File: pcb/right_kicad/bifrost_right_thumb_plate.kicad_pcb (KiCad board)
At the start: 2 copper layers, 47.3 x 36.4 mm, 2 parts

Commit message: Update PCB and case designs
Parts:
- PH44: value R0C43 -> 1U
- PH45: value R0C44 -> 1U
- moved PH45 202.1 mm to (99.2, 59.5), turned to 0 degrees
- moved PH44 200.9 mm to (79.8, 60.6), turned to 6.179 degrees
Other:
- board size 47.3 x 36.4 mm -> 49.9 x 21.9 mm
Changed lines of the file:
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@@
 		(legacy_teardrops no)
 	)
-	(paper "A3")
+	(paper "A5")
 	(layers
 		(0 "F.Cu" signal)
@@
 		(capping no)
 		(filling no)
-		(zone_defaults)
-		(grid_origin -102.4605 73.281)
 		(pcbplotparams
 			(layerselection 0x00000000_00000000_55555555_5755f5ff)
@@
 	(footprint "Smidr:Plate_Smidr_Key_Hole"
 		(layer "F.Cu")
-		(at -120.0205 81.69 28.679)
+		(at 79.77744 60.580232 6.179)
 		(descr "Smidr keyboard plate key hole, center-origin template")
 		(tags "Smidr keyboard plate key hole center origin")
 		(property "Reference" "PH44"
-			(at 0 -11.025 0)
+			(at 0.000001 -11.025 6.179)
 			(layer "F.SilkS")
 			(hide yes)
@@
 			)
 		)
-		(property "Value" "R0C43"
-			(at 0 11.025 0)
+		(property "Value" "1U"
+			(at 0 8.1 6.179)
+			(layer "F.Fab")
+			(effects
+				(font
+					(size 1 1)
+					(thickness 0.15)
+				)
+			)
+		)
+		(property "Datasheet" ""
+			(at 0 0 6.179)
 			(layer "F.Fab")
 			(hide yes)
 			(effects
 				(font
-					(size 1 1)
-					(thickness 0.15)
-				)
-			)
-		)
-		(property "Datasheet" ""
-			(at 0 0 0)
-			(layer "F.Fab")
-			(hide yes)
-			(effects
-				(font
 					(size 1.27 1.27)
 					(thickness 0.15)
@@
 		)
 		(property "Description" ""
-			(at 0 0 0)
+			(at 0 0 6.179)
 			(layer "F.Fab")
 			(hide yes)
@@
 		)
 		(fp_line
-			(start -7.05 6.550002)
+			(start -7.05 6.550003)
 			(end -7.05 -6.55)
 			(stroke
@@
 			(start -6.55 7.05)
 			(mid -6.903552 6.903554)
-			(end -7.05 6.550002)
+			(end -7.05 6.550003)
 			(stroke
 				(width 0.05)
@@
 			(start 6.55 -7.05)
 			(mid 6.903552 -6.903554)
-			(end 7.05 -6.550002)
+			(end 7.05 -6.550003)
 			(stroke
 				(width 0.05)
@@
 			(start 7.05 6.55)
 			(mid 6.903554 6.903552)
-			(end 6.550002 7.05)
+			(end 6.550003 7.05)
 			(stroke
 				(width 0.05)
@@
 			)
 			(stroke
-				(width 0.05)
-				(type solid)
-			)
-			(fill no)
-			(layer "F.CrtYd")
-		)
-		(fp_poly
-			(pts
-				(xy -9.525 -9.525) (xy 9.525 -9.525) (xy 9.525 9.525) (xy -9.525 9.525)
-			)
-			(stroke
 				(width 0.1)
 				(type solid)
@@
 	(footprint "Smidr:Plate_Smidr_Key_Hole"
 		(layer "F.Cu")
-		(at -102.4605 73.281 22.5)
+		(at 99.21875 59.53125)
 		(descr "Smidr keyboard plate key hole, center-origin template")
 		(tags "Smidr keyboard plate key hole center origin")
@@
 			)
 		)
-		(property "Value" "R0C44"
-			(at 0 11.025 0)
-			(layer "F.Fab")
-			(hide yes)
+		(property "Value" "1U"
+			(at 0 8.1 0)
+			(layer "F.Fab")
 			(effects
 				(font
@@
 		)
 		(fp_line
+			(start -7.05 6.550003)
+			(end -7.05 -6.55)
+			(stroke
+				(width 0.05)
+				(type solid)
+			)
+			(layer "Edge.Cuts")
+		)
+		(fp_line
 			(start -6.55 -7.05)
 			(end 6.55 -7.05)
@@
 		)
 		(fp_line
-			(start -7.05 6.550003)
-			(end -7.05 -6.55)
+			(start 6.55 7.05)
+			(end -6.55 7.05)
 			(stroke
 				(width 0.05)
@@
 			(start 7.05 -6.55)
 			(end 7.05 6.55)
-			(stroke
-				(width 0.05)
-				(type solid)
-			)
-			(layer "Edge.Cuts")
-		)
-		(fp_line
-			(start 6.55 7.05)
-			(end -6.55 7.05)
 			(stroke
 				(width 0.05)
@@
 			)
 			(stroke
-				(width 0.05)
+				(width 0.1)
 				(type solid)
 			)
 			(fill no)
-			(layer "F.CrtYd")
-		)
-		(fp_poly
-			(pts
-				(xy -9.525 -9.525) (xy 9.525 -9.525) (xy 9.525 9.525) (xy -9.525 9.525)
-			)
-			(stroke
-				(width 0.1)
-				(type solid)
-			)
-			(fill no)
 			(layer "F.Fab")
 		)
@@
 	)
 	(gr_arc
-		(start -133.089803 78.8872)
-		(mid -133.204233 77.830235)
-		(end -132.537762 77.001931)
+		(start 68.775564 52.989377)
+		(mid 69.074328 51.969078)
+		(end 70.007045 51.458872)
 		(stroke
 			(width 0.1)
@@
 	)
 	(gr_line
-		(start -133.089803 78.8872)
-		(end -125.852286 92.118317)
+		(start 68.775564 52.989377)
+		(end 70.398829 67.983013)
+		(stroke
+			(width 0.1)
+			(type default)
+		)
+		(layer "Edge.Cuts")
+	)
+	(gr_arc
+		(start 74.553053 71.325606)
+		(mid 71.783666 70.514679)
+		(end 70.398829 67.983013)
 		(stroke
 			(width 0.1)
@@
 	)
 	(gr_line
-		(start -124.877641 72.811792)
-		(end -132.537762 77.001931)
-		(stroke
-			(width 0.1)
-			(type default)
-		)
-		(layer "Edge.Cuts")
-	)
-	(gr_arc
-		(start -124.877641 72.811792)
-		(mid -107.408552 64.380257)
-		(end -89.173486 57.766465)
-		(stroke
-			(width 0.1)
-			(type default)
-		)
-		(layer "Edge.Cuts")
-	)
-	(gr_arc
-		(start -120.735128 93.616718)
-		(mid -123.604037 93.927318)
-		(end -125.852286 92.118317)
+		(start 74.553053 71.325606)
+		(end 80.866162 70.642126)
 		(stroke
 			(width 0.1)
@@
 	)
 	(gr_line
-		(start -120.735128 93.616718)
-		(end -115.164132 90.569342)
-		(stroke
-			(width 0.1)
-			(type default)
-		)
-		(layer "Edge.Cuts")
-	)
-	(gr_arc
-		(start -115.164132 90.569342)
-		(mid -101.298584 83.781393)
-		(end -86.875913 78.275375)
-		(stroke
-			(width 0.1)
-			(type default)
-		)
-		(layer "Edge.Cuts")
-	)
-	(gr_arc
-		(start -89.173486 57.766465)
-		(mid -87.670587 58.241659)
-		(end -87.579323 59.815249)
-		(stroke
-			(width 0.1)
-			(type default)
-		)
-		(layer "Edge.Cuts")
-	)
-	(gr_arc
-		(start -86.256776 76.053326)
-		(mid -89.548592 68.148538)
-		(end -87.579323 59.815249)
-		(stroke
-			(width 0.1)
-			(type default)
-		)
-		(layer "Edge.Cuts")
-	)
-	(gr_arc
-		(start -86.256776 76.053326)
-		(mid -85.973982 77.329403)
-		(end -86.875913 78.275375)
-		(stroke
-			(width 0.1)
+		(start 78.68757 50.51909)
+		(end 70.007045 51.458872)
+		(stroke
+			(width 0.1)
+			(type default)
+		)
+		(layer "Edge.Cuts")
+	)
+	(gr_arc
+		(start 78.68757 50.51909)
+		(mid 98.053513 49.414498)
+		(end 117.431506 50.282409)
+		(stroke
+			(width 0.1)
+			(type default)
+		)
+		(layer "Edge.Cuts")
+	)
+	(gr_arc
+		(start 80.866162 70.642126)
+		(mid 96.273894 69.676994)
+		(end 111.705766 70.109414)
+		(stroke
+			(width 0.1)
+			(type default)
+		)
+		(layer "Edge.Cuts")
+	)
+	(gr_arc
+		(start 113.128116 68.293442)
+		(mid 112.90105 69.580604)
+		(end 111.705766 70.109414)
+		(stroke
+			(width 0.1)
+			(type default)
+		)
+		(layer "Edge.Cuts")
+	)
+	(gr_arc
+		(start 113.128116 68.293442)
+		(mid 113.111906 59.730647)
+		(end 118.120285 52.785298)
+		(stroke
+			(width 0.1)
+			(type default)
+		)
+		(layer "Edge.Cuts")
+	)
+	(gr_arc
+		(start 117.431506 50.282409)
+		(mid 118.638155 51.296565)
+		(end 118.120285 52.785298)
+		(stroke
+			(width 0.1)

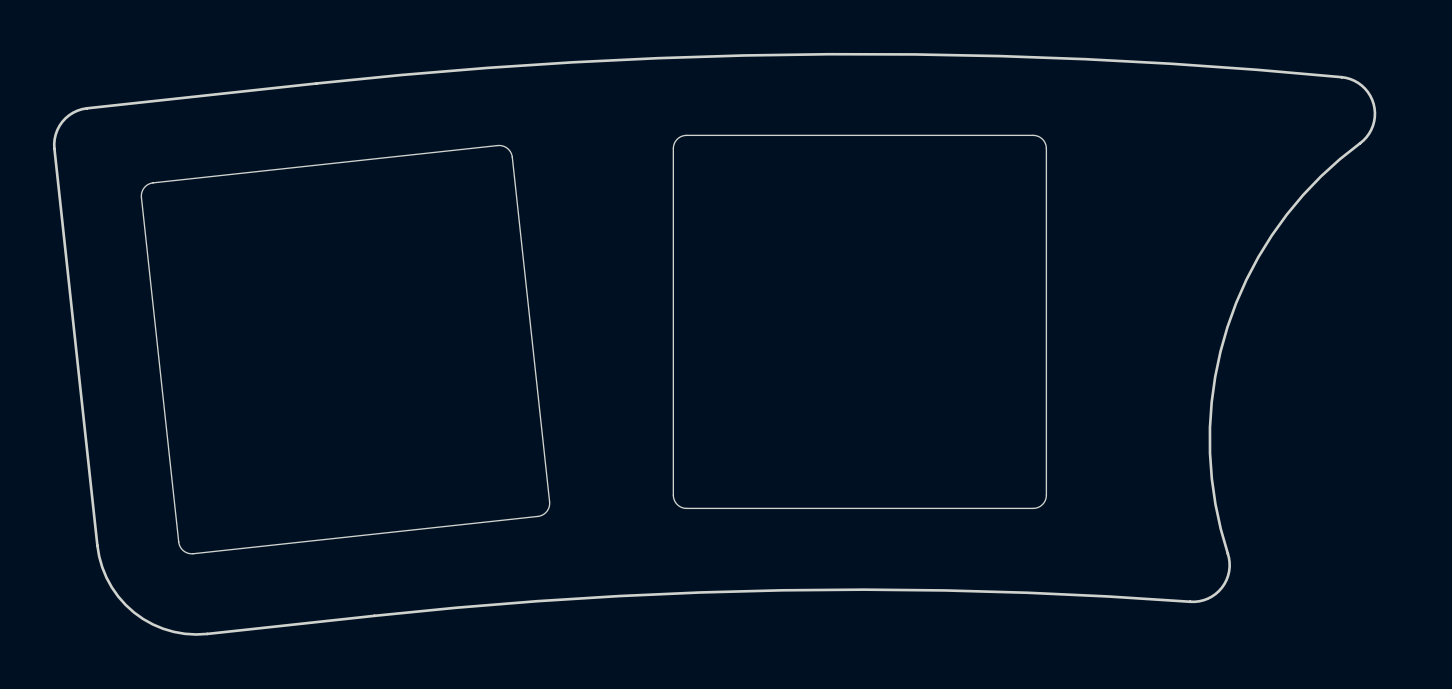
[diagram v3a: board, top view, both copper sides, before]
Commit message: Update case and plate designs
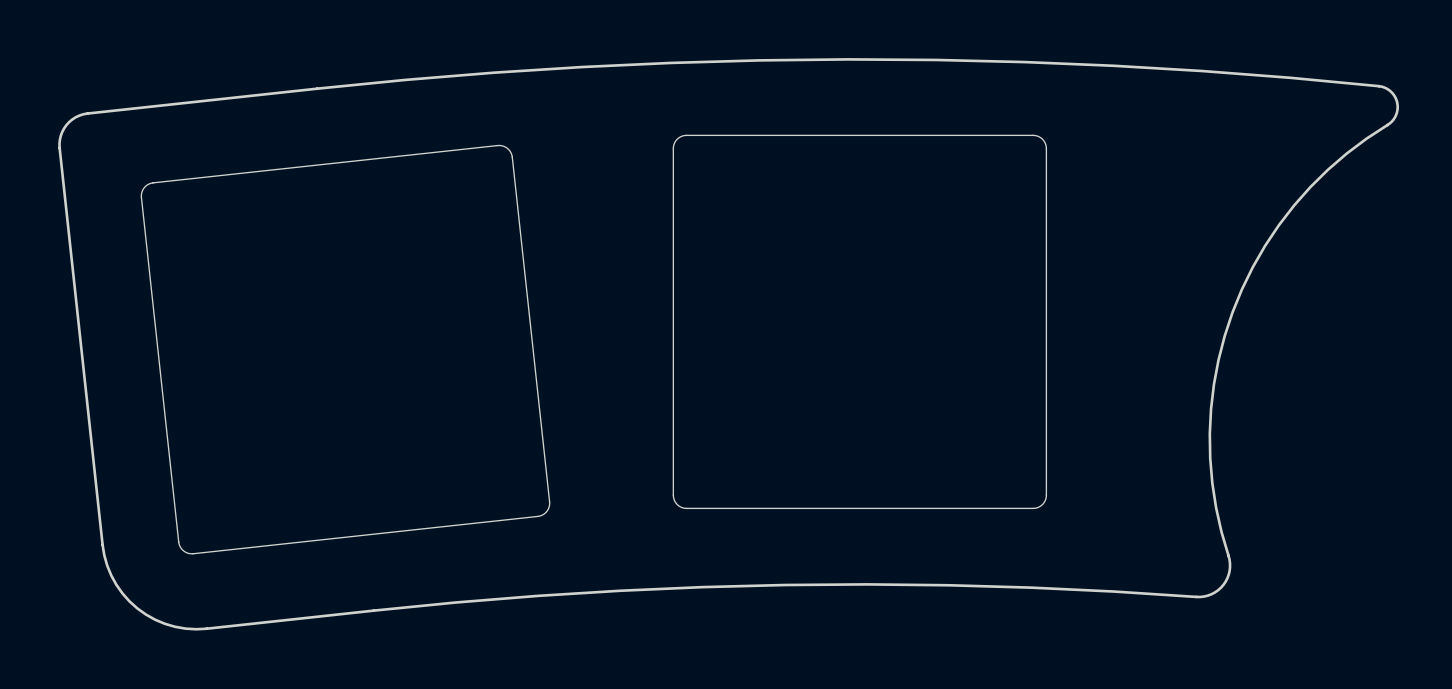
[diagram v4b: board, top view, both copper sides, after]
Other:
- board size 49.9 x 21.9 mm -> 50.6 x 21.5 mm
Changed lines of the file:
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@@
 	)
 	(gr_arc
-		(start 68.775564 52.989377)
-		(mid 69.074328 51.969078)
-		(end 70.007045 51.458872)
+		(start 68.972849 52.968019)
+		(mid 69.228932 52.093475)
+		(end 70.028406 51.656157)
 		(stroke
 			(width 0.1)
@@
 	)
 	(gr_line
-		(start 68.775564 52.989377)
-		(end 70.398829 67.983013)
+		(start 68.972849 52.968019)
+		(end 70.596113 67.961655)
 		(stroke
 			(width 0.1)
@@
 	)
 	(gr_arc
-		(start 74.553053 71.325606)
-		(mid 71.783666 70.514679)
-		(end 70.398829 67.983013)
+		(start 74.531696 71.128323)
+		(mid 71.908065 70.360076)
+		(end 70.596113 67.961655)
 		(stroke
 			(width 0.1)
@@
 	)
 	(gr_line
-		(start 74.553053 71.325606)
-		(end 80.866162 70.642126)
+		(start 74.531696 71.128323)
+		(end 80.844803 70.444842)
 		(stroke
 			(width 0.1)
@@
 	)
 	(gr_line
-		(start 78.68757 50.51909)
-		(end 70.007045 51.458872)
+		(start 78.708931 50.716375)
+		(end 70.028406 51.656157)
 		(stroke
 			(width 0.1)
@@
 	)
 	(gr_arc
-		(start 78.68757 50.51909)
-		(mid 98.053513 49.414498)
-		(end 117.431506 50.282409)
+		(start 78.708931 50.716375)
+		(mid 98.769198 49.609907)
+		(end 118.834462 50.621708)
 		(stroke
 			(width 0.1)
@@
 	)
 	(gr_arc
-		(start 80.866162 70.642126)
-		(mid 96.273894 69.676994)
-		(end 111.705766 70.109414)
+		(start 80.844803 70.444842)
+		(mid 96.377063 69.47678)
+		(end 111.932941 69.927258)
 		(stroke
 			(width 0.1)
@@
 	)
 	(gr_arc
-		(start 113.128116 68.293442)
-		(mid 112.90105 69.580604)
-		(end 111.705766 70.109414)
+		(start 113.15157 68.36471)
+		(mid 112.960476 69.472154)
+		(end 111.932941 69.927258)
 		(stroke
 			(width 0.1)
@@
 	)
 	(gr_arc
-		(start 113.128116 68.293442)
-		(mid 113.111906 59.730647)
-		(end 118.120285 52.785298)
+		(start 113.15157 68.36471)
+		(mid 113.304177 59.174093)
+		(end 119.162568 52.091015)
 		(stroke
 			(width 0.1)
@@
 	)
 	(gr_arc
-		(start 117.431506 50.282409)
-		(mid 118.638155 51.296565)
-		(end 118.120285 52.785298)
+		(start 118.834462 50.621708)
+		(mid 119.527426 51.238253)
+		(end 119.162568 52.091015)
 		(stroke
 			(width 0.1)
@@
 	)
 	(group ""
-		(members "131f2e45-1469-442b-b1c3-38125ea1bc75" "283b4b28-6431-4de2-926f-d4100385ad36"
-			"37530035-962f-450e-808b-76fc856d540e" "3ea7d064-ed18-4127-98e1-dce7d881c859"
-			"68696686-0b29-424a-97d3-32e8162fcf36" "9d30e770-3ff9-421a-81a0-abc2ab325a40"
-			"9db6b27a-5fb6-459c-b513-9c9523398cd3" "9ed6bb4c-fc6f-4d4d-b85e-132a77d1c42d"
-			"eddd10f2-df02-4562-b401-ab70a6a116ae" "f8a689c5-95bd-42cb-8c69-a766b9aa7194"
+		(members "1dc7199f-a0dc-4f2f-a28a-05933beafd66" "21ff6396-de92-4f08-b400-14a7e8ff70ca"
+			"410fb3e4-1a40-45c4-a949-ce1cec9de1eb" "47bad8f2-c720-4961-8c14-10fe7af8c936"
+			"49f489a2-6ad3-4b33-bef2-56069933c145" "4f11038b-4a59-4dff-b6e3-5b25e45f2649"
+			"5ecb0989-6ae5-46da-bca6-fcc61dd4f9fb" "9ecb11cf-6a1d-4343-a14a-78af8804b90b"
+			"a9ad33b2-a113-4c2e-b73c-eb1547c66c0e" "b0437012-b7fb-4e12-bfc3-6c206d164417"
 		)
 	)
